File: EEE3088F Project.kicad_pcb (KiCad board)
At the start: 2 copper layers, 58 parts, among them J1 Conn_02x16_Odd_Even, J2 Battery IN JST, M1Control1 DRV8837, M2Control1 DRV8837, M3Control1 DRV8837, M4Control1 DRV8837, Q2 AO3400A, U1 TP4056, U2 TPS62163DSG, U3 MT3608, U5 TPS62162DSG, U6 CH224K

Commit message: changed inductors
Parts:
- removed L3: 2.2uH, Inductor_SMD:L_Taiyo-Yuden_MD-3030
- added L4: 3.3uH, Custom Footprints:IND-SMD_L4.0-W4.0_FNR40XXS, F.Cu at (156.6, 91.3)
- added OverCurrentFlag2TP1: TestPoint, TestPoint:TestPoint_Pad_2.0x2.0mm, F.Cu at (155.8, 77.1)
- added OvercurrentFlag1TP1: TestPoint, TestPoint:TestPoint_Pad_2.0x2.0mm, F.Cu at (155.8, 81.1)
- added TP1: 5V_test, TestPoint:TestPoint_Pad_2.0x2.0mm, F.Cu at (159.8, 77.1)
- added TP2: USBC9V_test, TestPoint:TestPoint_Pad_2.0x2.0mm, F.Cu at (159.8, 81.1)
- added TP3: below_10k_test, TestPoint:TestPoint_Pad_2.0x2.0mm, F.Cu at (163.9, 77.1)
- added TP4: 5V_out_test, TestPoint:TestPoint_Pad_2.0x2.0mm, F.Cu at (163.9, 81.1)
- added TP5: 3V3_out_test, TestPoint:TestPoint_Pad_2.0x2.0mm, F.Cu at (167.9, 77.1)
- added UnusedPinTP1: TestPoint, TestPoint:TestPoint_Pad_2.0x2.0mm, F.Cu at (167.9, 81.1)
- L1: value 2.2uH -> 10uH; footprint Inductor_SMD:L_Taiyo-Yuden_MD-3030 -> Custom Footprints:IND-SMD_L7.8-W7.0-A
- L2: value 2.2uH -> 3.3uH; footprint Inductor_SMD:L_Taiyo-Yuden_MD-3030 -> Custom Footprints:IND-SMD_L4.0-W4.0_FNR40XXS
- moved L1 67.1 mm to (164.3, 87.5)
- moved L2 64.4 mm to (156.6, 85.9)
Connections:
- net /5V_out renamed /5V Regulated
- C11 pad 2: Net-(JP2-B) -> /3V3 Regulated
- C15 pad 1: /3V3_out -> /3V3 Regulated
- C2 pad 1: VBatt -> VCharge
- C3 pad 1: VBUS -> 9V USB-C
- C6 pad 2: Net-(JP2-B) -> /3V3 Regulated
- C7 pad 2: Net-(JP2-B) -> /3V3 Regulated
- C9 pad 2: Net-(JP2-B) -> /3V3 Regulated
- CurrentSensor1 pad 2: VBatt -> /RSense-
- J1 pad 12: unconnected-(J1-Pin_12-Pad12) -> /USART2_TX
- J1 pad 15: unconnected-(J1-Pin_15-Pad15) -> Net-(J1-Pin_15)
- J1 pad 18: /3V3_out -> /3V3 Regulated
- J1 pad 22: unconnected-(J1-Pin_22-Pad22) -> 9V USB-C
- J1 pad 23: unconnected-(J1-Pin_23-Pad23) -> GND
- J1 pad 9: unconnected-(J1-Pin_9-Pad9) -> /USART2_RX
- J2 pad 2: Net-(J2-Pin_2) -> /RSense+
- L1 pad 1: Net-(U2-SW) -> VBatt
- L1 pad 2: Net-(D2-A) -> Net-(D1-A)
- L2 pad 2: /3V3_out -> /3V3 Regulated
- M1Control1 pad 8: Net-(JP2-B) -> /3V3 Regulated
- M2Control1 pad 8: Net-(JP2-B) -> /3V3 Regulated
- M3Control1 pad 8: Net-(JP2-B) -> /3V3 Regulated
- M4Control1 pad 8: Net-(JP2-B) -> /3V3 Regulated
- R6 pad 1: VBUS -> 9V USB-C
- R7 pad 2: /3V3_out -> /3V3 Regulated
- RSense1 pad 1: VBatt -> /RSense-
- RSenseTP-1 pad 1: VBatt -> /RSense-
- SWPwr1 pad 1: /RSense+ -> VBatt
- SWPwr1 pad 2: Net-(J2-Pin_2) -> /RSense-
- SWPwr1 pad 3: Net-(SWPwr1-C) -> VCharge
- U1 pad 5: VBatt -> VCharge
- U2 pad 2: VBUS -> 9V USB-C
- U2 pad 3: VBUS -> 9V USB-C
- U5 pad 6: /3V3_out -> /3V3 Regulated

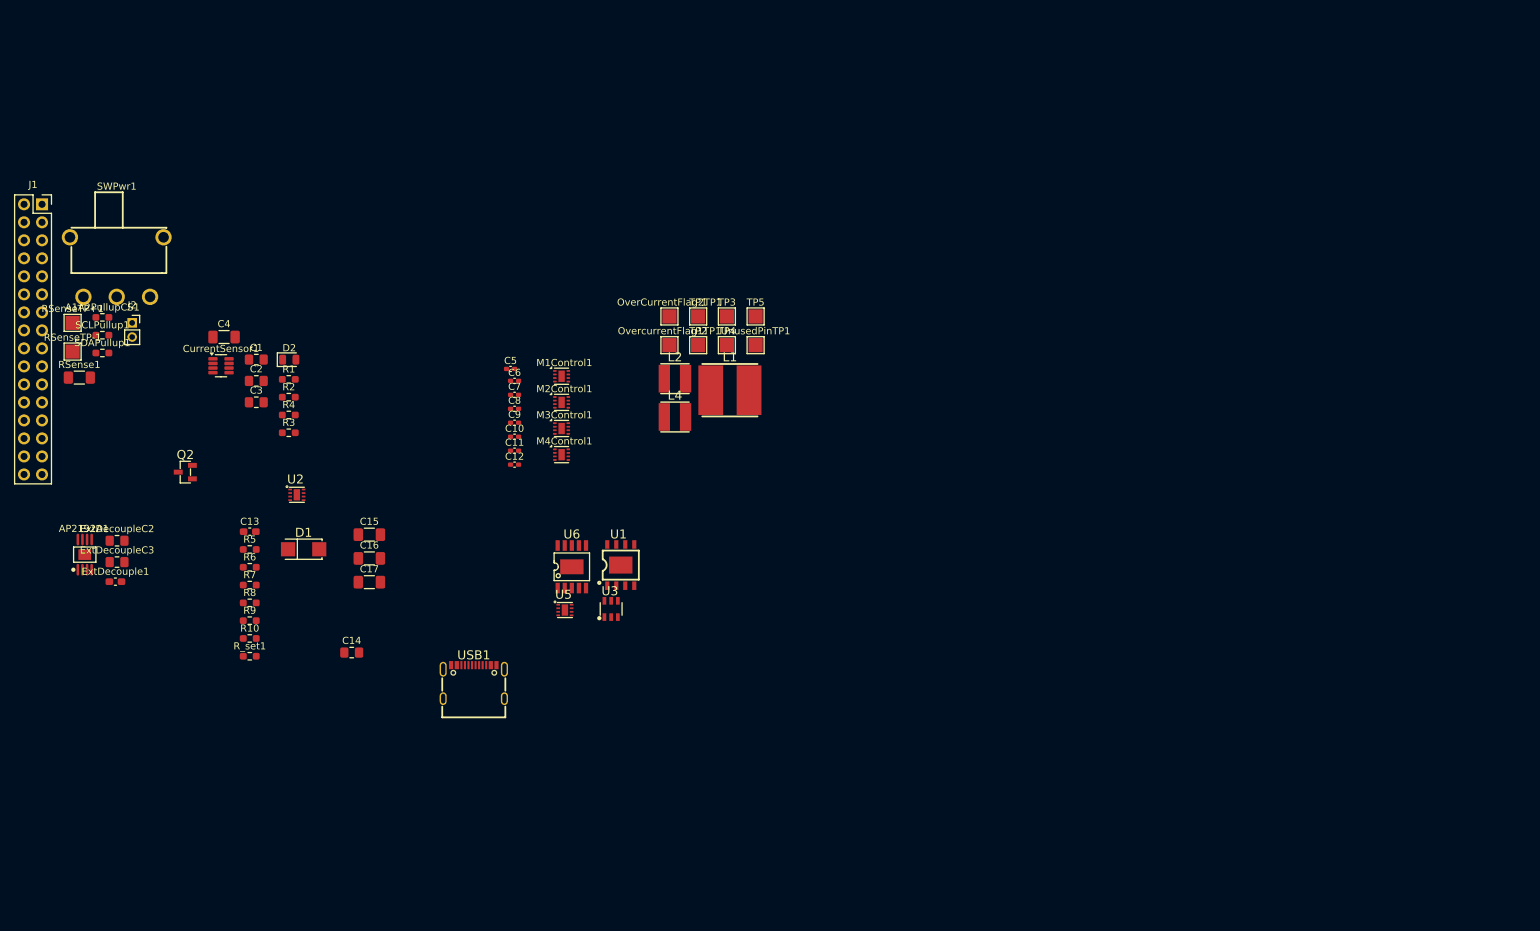
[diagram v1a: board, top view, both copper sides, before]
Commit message: Routed Thomas half of PCB traces. Minor labelling modifications in schematic.
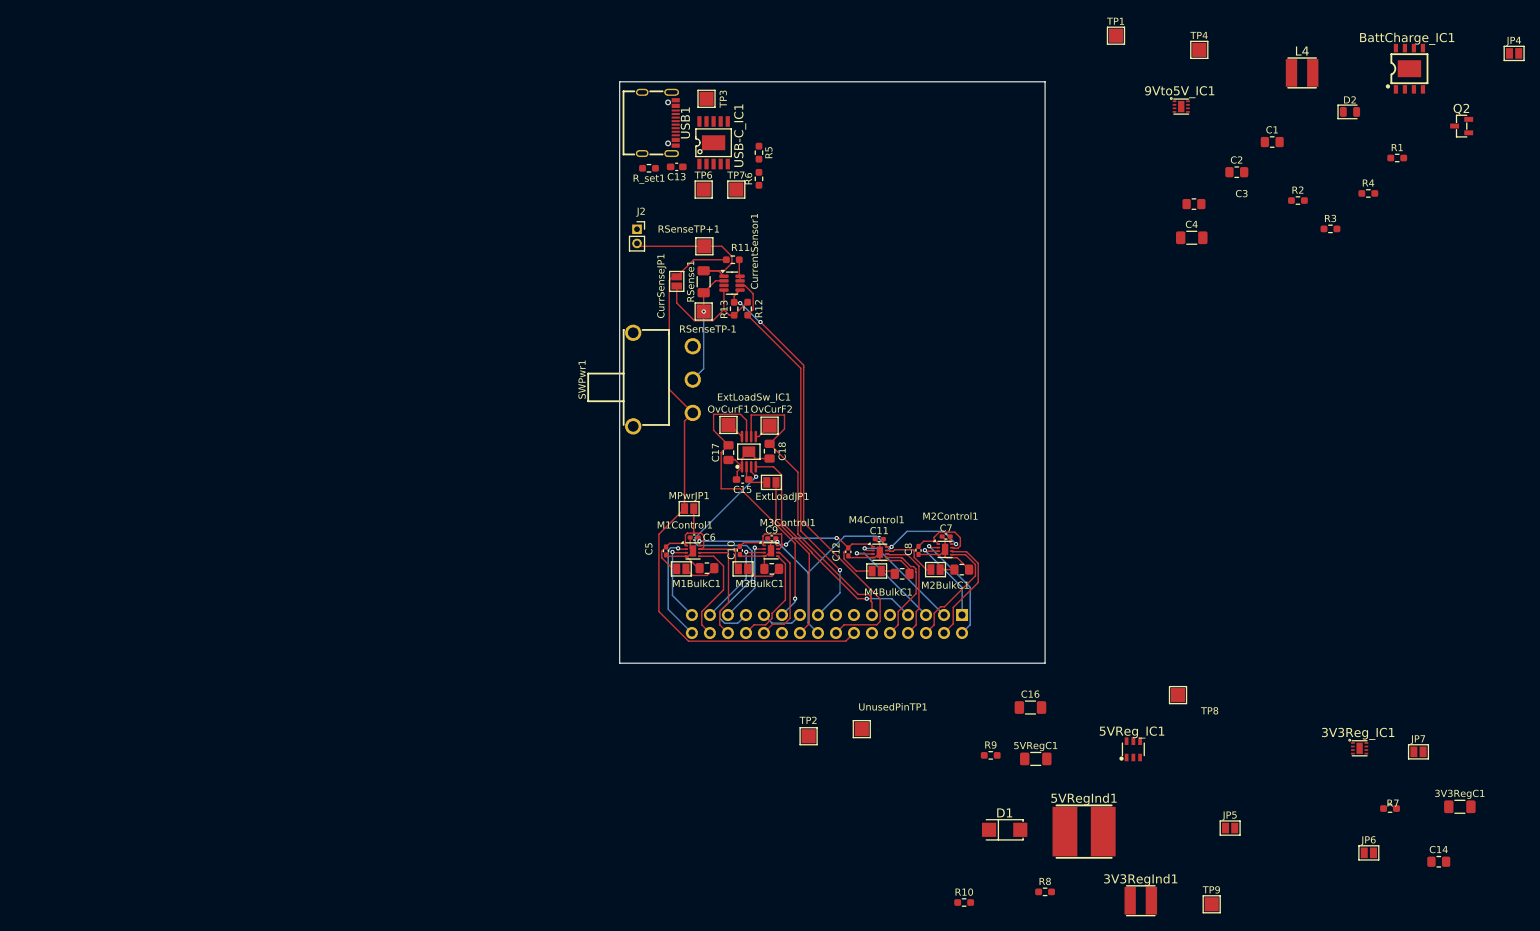
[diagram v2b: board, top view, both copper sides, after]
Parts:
- removed TP5: 3V3_out_test, TestPoint:TestPoint_Pad_2.0x2.0mm
- added CurrSenseJP1: CurrentSenseJP, Jumper:SolderJumper-2_P1.3mm_Open_Pad1.0x1.5mm, F.Cu at (156.8, 72.2)
- added ExtLoadJP1: ExtLoadJP, Jumper:SolderJumper-2_P1.3mm_Open_Pad1.0x1.5mm, F.Cu at (170.2, 100.5)
- added JP10: BCM2_JP, Jumper:SolderJumper-2_P1.3mm_Open_Pad1.0x1.5mm, F.Cu at (193.3, 112.8)
- added JP11: BCM1_JP, Jumper:SolderJumper-2_P1.3mm_Open_Pad1.0x1.5mm, F.Cu at (157.4, 112.7)
- added JP4: ChargeJP, Jumper:SolderJumper-2_P1.3mm_Open_Pad1.0x1.5mm, F.Cu at (274.9, 40.0)
- added JP5: 5VRegInJP, Jumper:SolderJumper-2_P1.3mm_Open_Pad1.0x1.5mm, F.Cu at (234.8, 149.2)
- added JP6: 3V3RegInJP, Jumper:SolderJumper-2_P1.3mm_Open_Pad1.0x1.5mm, F.Cu at (254.4, 152.8)
- added JP7: 3V3RegOutJP, Jumper:SolderJumper-2_P1.3mm_Open_Pad1.0x1.5mm, F.Cu at (261.4, 138.5)
- added JP8: BCM4_JP, Jumper:SolderJumper-2_P1.3mm_Open_Pad1.0x1.5mm, F.Cu at (185.0, 113.0)
- added M1BulkC1: 10uF, Capacitor_SMD:C_0805_2012Metric_Pad1.18x1.45mm_HandSolder, F.Cu at (161.1, 112.6)
- added M2BulkC1: 10uF, Capacitor_SMD:C_0805_2012Metric_Pad1.18x1.45mm_HandSolder, F.Cu at (197.0, 112.8)
- added M3BC1: BCM3_JP, Jumper:SolderJumper-2_P1.3mm_Open_Pad1.0x1.5mm, F.Cu at (166.2, 112.7)
- added M3BulkC1: 10uF, Capacitor_SMD:C_0805_2012Metric_Pad1.18x1.45mm_HandSolder, F.Cu at (170.2, 112.7)
- added M4BulkC1: 10uF, Capacitor_SMD:C_0805_2012Metric_Pad1.18x1.45mm_HandSolder, F.Cu at (188.6, 113.4)
- added MPwrJP1: MotorPWRJP, Jumper:SolderJumper-2_P1.3mm_Open_Pad1.0x1.5mm, F.Cu at (158.6, 104.2)
- added TP6: DP_TP, TestPoint:TestPoint_Pad_2.0x2.0mm, F.Cu at (160.6, 59.2)
- added TP7: DM_TP, TestPoint:TestPoint_Pad_2.0x2.0mm, F.Cu at (165.2, 59.2)
- added TP8: 5VRegDiv_TP2, TestPoint:TestPoint_Pad_2.0x2.0mm, F.Cu at (227.5, 130.5)
- added TP9: 5VRegDiv_TP1, TestPoint:TestPoint_Pad_2.0x2.0mm, F.Cu at (232.2, 160.0)
- J1: moved to B.Cu
- TP1: value 5V_test -> 5V_TP
- TP2: value USBC9V_test -> USBC9V_TP
- TP3: value below_10k_test -> below_10k_TP
- moved Q2 186.5 mm to (267.5, 50.2)
- moved R7 163.9 mm to (257.4, 146.5)
- moved R1 159.4 mm to (258.4, 54.8)
- moved 3V3RegC1 158.5 mm to (267.2, 146.2)
- moved C14 156.1 mm to (264.3, 154.0)
- moved R4 155.4 mm to (254.3, 59.8)
- moved D2 153.6 mm to (251.8, 48.2)
- moved R3 149.7 mm to (249.0, 64.8)
- moved C1 146.5 mm to (240.8, 52.5)
- moved R2 145.0 mm to (244.4, 60.8)
- moved J1 142.1 mm to (197.0, 119.2), turned to 90 degrees
- moved C2 141.4 mm to (235.8, 56.8)
- moved C4 137.2 mm to (229.4, 66.0)
- moved 9Vto5V_IC1 136.2 mm to (227.9, 47.5)
- moved C3 135.2 mm to (229.8, 61.2)
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- renumbered C15 to 3V3RegC1, L2 to 3V3RegInd1, U5 to 3V3Reg_IC1, C17 to 5VRegC1, L1 to 5VRegInd1, U3 to 5VReg_IC1, U2 to 9Vto5V_IC1, U1 to BattCharge_IC1, ExtDecouple1 to C15, ExtDecoupleC2 to C17, ExtDecoupleC3 to C18, AP2192A1 to ExtLoadSw_IC1, OvercurrentFlag1TP1 to OvCurF1, OverCurrentFlag2TP1 to OvCurF2, A1A2PullupCS1 to R11, SDAPullup1 to R12, SCLPullup1 to R13, U6 to USB-C_IC1
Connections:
- 3V3RegC1 pad 1: /3V3 Regulated -> Net-(3V3Reg_IC1-VOS)
- 3V3RegInd1 pad 2: /3V3 Regulated -> Net-(3V3Reg_IC1-VOS)
- 3V3Reg_IC1 pad 2: /5V Regulated -> Net-(3V3Reg_IC1-EN)
- 3V3Reg_IC1 pad 3: /5V Regulated -> Net-(3V3Reg_IC1-EN)
- 3V3Reg_IC1 pad 6: /3V3 Regulated -> Net-(3V3Reg_IC1-VOS)
- 5VRegInd1 pad 1: VBatt -> Net-(5VReg_IC1-EN)
- 5VReg_IC1 pad 4: VBatt -> Net-(5VReg_IC1-EN)
- 5VReg_IC1 pad 5: VBatt -> Net-(5VReg_IC1-EN)
- 9Vto5V_IC1 pad 2: 9V USB-C -> Net-(9Vto5V_IC1-EN)
- 9Vto5V_IC1 pad 3: 9V USB-C -> Net-(9Vto5V_IC1-EN)
- C10 pad 1: Net-(JP2-B) -> Net-(JP10-A)
- C12 pad 1: Net-(JP2-B) -> Net-(JP10-A)
- C14 pad 1: /5V Regulated -> Net-(3V3Reg_IC1-EN)
- C16 pad 1: VBatt -> Net-(5VReg_IC1-EN)
- C3 pad 1: 9V USB-C -> Net-(9Vto5V_IC1-EN)
- C5 pad 1: Net-(JP2-B) -> Net-(JP10-A)
- C8 pad 1: Net-(JP2-B) -> Net-(JP10-A)
- J1 pad 1: /MOTOR2_B_OUT -> /MOTOR2_B_OUT 
- J1 pad 19: unconnected-(J1-Pin_19-Pad19) -> GND
- J1 pad 6: /MOTOR2_CTRL2  -> /MOTOR2_CTRL2
- J1 pad 8: /MOTOR4_CTRL1  -> /MOTOR4_CTRL1
- M1Control1 pad 1: Net-(JP2-B) -> Net-(JP10-A)
- M1Control1 pad 7: VBatt -> Net-(JP10-A)
- M2Control1 pad 1: Net-(JP2-B) -> Net-(JP10-A)
- M2Control1 pad 7: VBatt -> Net-(JP10-A)
- M3Control1 pad 1: Net-(JP2-B) -> Net-(JP10-A)
- M3Control1 pad 7: VBatt -> Net-(JP10-A)
- M4Control1 pad 1: Net-(JP2-B) -> Net-(JP10-A)
- M4Control1 pad 3: /MOTOR4_B_OUT  -> /MOTOR4_B_OUT
- M4Control1 pad 7: VBatt -> Net-(JP10-A)
- R7 pad 2: /3V3 Regulated -> Net-(3V3Reg_IC1-VOS)
- USB-C_IC1 pad 4: unconnected-(U6-DP-Pad4) -> Net-(USB-C_IC1-DP)
- USB-C_IC1 pad 5: unconnected-(U6-DM-Pad5) -> Net-(USB-C_IC1-DM)
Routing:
- net VBatt: track 0.00 -> 89.0 mm
- net Net-(JP10-A): track 0.00 -> 77.0 mm, vias 0 -> 2
- net /12C1_SCL: track 0.00 -> 63.3 mm, vias 0 -> 2
- net /3V3 Regulated: track 0.00 -> 60.6 mm, vias 0 -> 4
- net GND: track 0.00 -> 58.5 mm
- net /12C1_SDA: track 0.00 -> 54.6 mm, vias 0 -> 1
- net /EXT_LOAD2_OUT: track 0.00 -> 43.7 mm
- net /EXT_LOAD1_OUT: track 0.00 -> 43.6 mm, vias 0 -> 1
- net /CTRL_EXT_LOAD1: track 0.00 -> 38.9 mm, vias 0 -> 1
- net /CTRL_EXT_LOAD2: track 0.00 -> 34.1 mm, vias 0 -> 1
- net /5V Regulated: track 0.00 -> 23.7 mm
- net /RSense+: track 0.00 -> 22.7 mm
- net Net-(CurrSenseJP1-A): track 0.00 -> 17.9 mm
- net /MOTOR2_CTRL2: track 0.00 -> 16.7 mm
- net /MOTOR2_A_OUT: track 0.00 -> 16.5 mm, vias 0 -> 1
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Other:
- board outline added: 60 x 82 mm

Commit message: finished routing
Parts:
- moved C14 104.5 mm to (178.0, 95.1), turned to -90 degrees
- moved 3V3RegPinJP 98.8 mm to (179.5, 88.3), turned to 90 degrees
- moved ChargeJP 96.6 mm to (179.3, 54.0)
- moved 5VRegInJP 94.9 mm to (176.3, 74.5), turned to 180 degrees
- moved 3V3RegC1 90.4 mm to (194.2, 93.0), turned to -90 degrees
- moved R7 88.2 mm to (185.5, 95.3), turned to -90 degrees
- moved 5VRegDiv_TP1 85.4 mm to (200.5, 80.8)
- moved USBC9V_TP 85.1 mm to (173.2, 51.2)
- moved 3V3Reg_IC1 83.0 mm to (181.9, 95.3)
- moved R1 82.3 mm to (176.9, 66.5)
- moved BattCharge_IC1 79.2 mm to (184.0, 64.0), turned to 90 degrees
- moved CHRG_LED 76.8 mm to (176.5, 63.5), turned to 90 degrees
- moved 5VRegInd1 76.6 mm to (197.5, 75.0)
- moved 3V3RegInd1 76.0 mm to (189.2, 91.0)
- moved AO3400A 75.4 mm to (193.5, 64.5), turned to -90 degrees
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- renumbered JP7 to 3V3RegOutJP, JP6 to 3V3RegPinJP, TP4 to 5VOutTest_TP, TP9 to 5VRegDiv_TP1, TP8 to 5VRegDiv_TP2, JP5 to 5VRegInJP, TP1 to 5V_TP, Q2 to AO3400A, D2 to CHRG_LED, JP4 to ChargeJP, TP7 to DM_TP, TP6 to DP_TP, D1 to D_S, USB-C_IC1 to USB-C_IC, USB1 to USB-TYPEC-16PIN, TP2 to USBC9V_TP, TP3 to below_10k_TP
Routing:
- net GND: track 58.5 -> 226.3 mm, vias 0 -> 10
- net 9V USB-C: track 0.00 -> 133.9 mm, vias 0 -> 1
- net /FAST_CHRG_CNTRL: track 0.00 -> 130.3 mm, vias 0 -> 1
- net Net-(9Vto5V_IC1-VOS): track 0.00 -> 68.4 mm, vias 0 -> 2
- net /5V Regulated: track 23.7 -> 91.7 mm, vias 0 -> 4
- net VCharge: track 0.00 -> 67.3 mm, vias 0 -> 4
- net /3V3 Regulated: track 60.6 -> 122.5 mm, vias 4 -> 7
- net Net-(5VReg_IC1-SW): track 0.00 -> 43.2 mm, vias 0 -> 2
- net Net-(5VReg_IC1-FB): track 0.00 -> 40.0 mm
- net Net-(3V3Reg_IC1-VOS): track 0.00 -> 35.7 mm
- net Net-(J1-Pin_15): track 0.00 -> 32.0 mm, vias 0 -> 2
- net Net-(USB-C_IC1-VBUS): track 0.00 -> 28.3 mm
- net /VBUS_USBC: track 0.00 -> 22.9 mm
- net Net-(5VReg_IC1-EN): track 0.00 -> 20.3 mm
- net VBatt: track 89.0 -> 109.1 mm, vias 0 -> 4
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
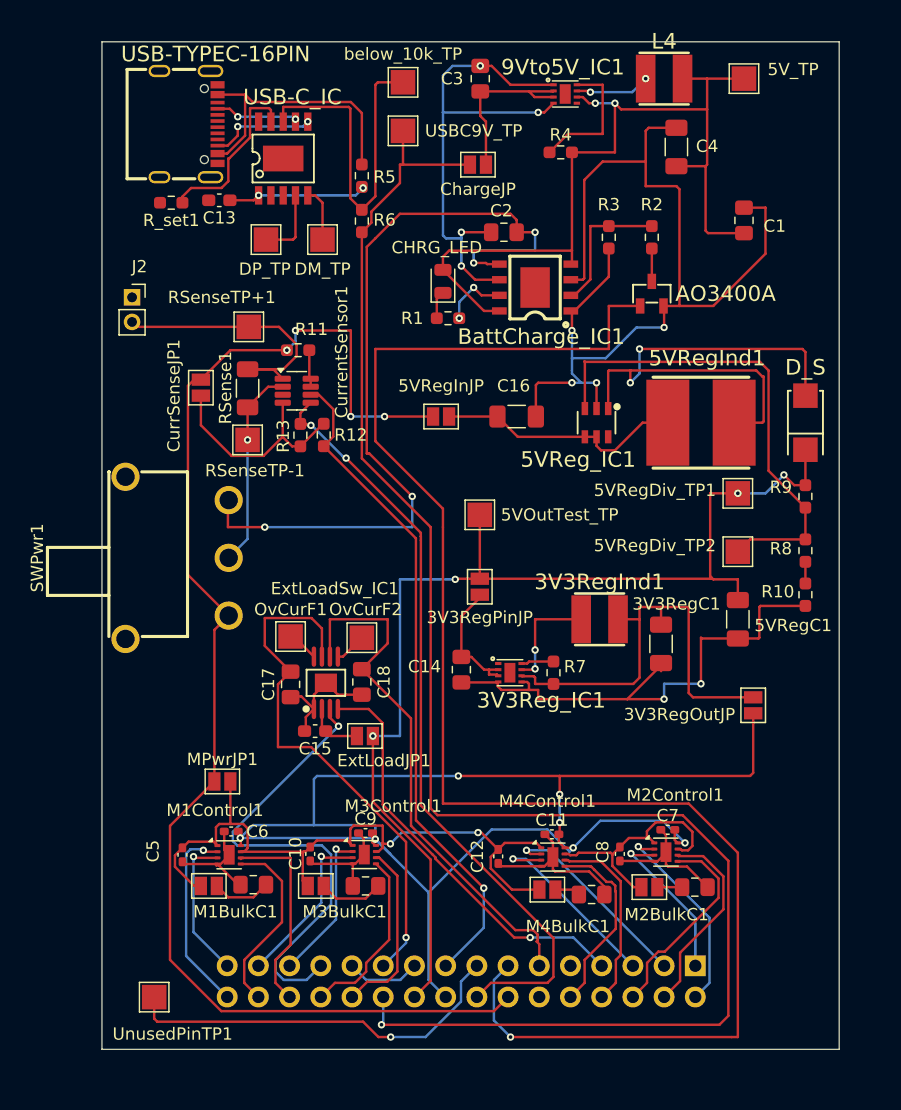
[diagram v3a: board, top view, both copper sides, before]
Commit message: added and fixed traces and trace widths. Fixed design rule check errors
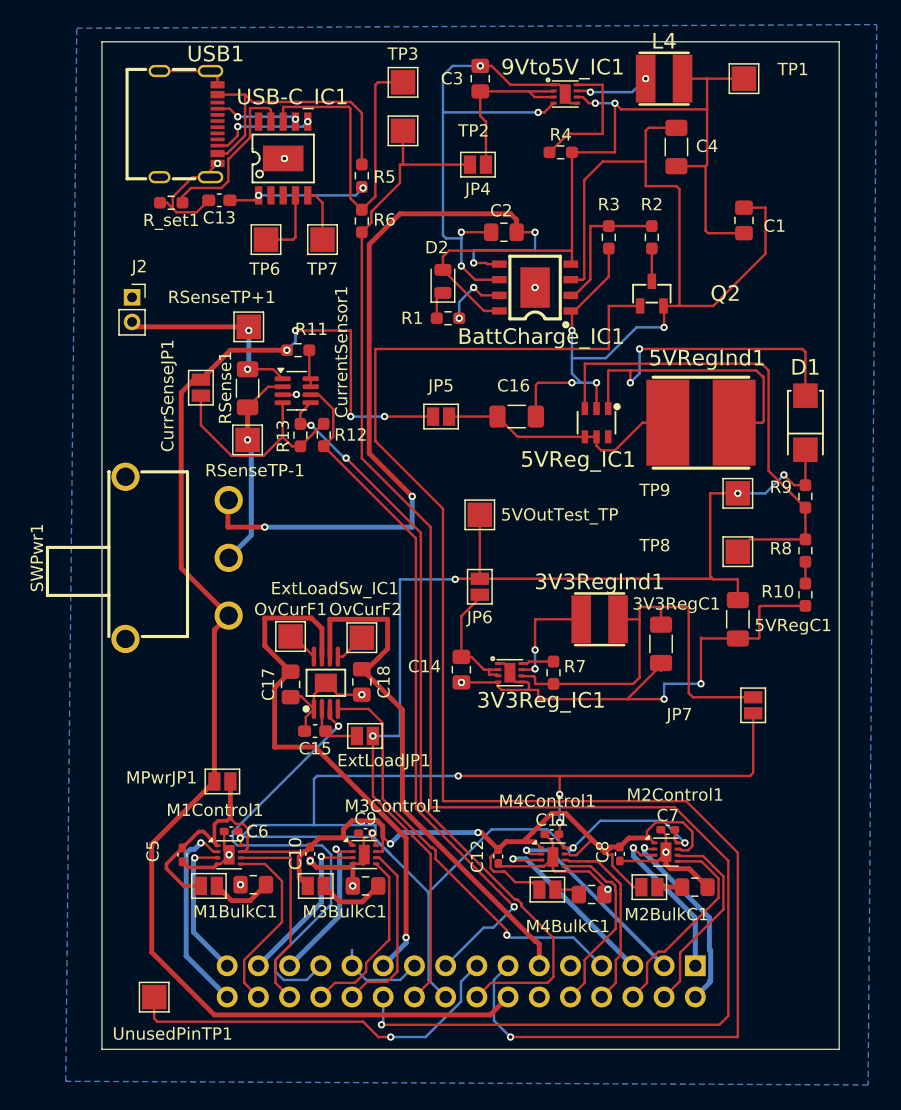
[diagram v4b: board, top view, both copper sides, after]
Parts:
- renumbered M3BC1 to BCM3_JP1, D_S to D1, CHRG_LED to D2, ChargeJP to JP4, 5VRegInJP to JP5, 3V3RegPinJP to JP6, 3V3RegOutJP to JP7, AO3400A to Q2, 5V_TP to TP1, USBC9V_TP to TP2, below_10k_TP to TP3, DP_TP to TP6, DM_TP to TP7, 5VRegDiv_TP2 to TP8, 5VRegDiv_TP1 to TP9, USB-C_IC to USB-C_IC1, USB-TYPEC-16PIN to USB1
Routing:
- net GND: track 226.3 -> 251.2 mm, vias 10 -> 22
- net Net-(BCM3_JP1-A): track 77.0 -> 89.3 mm
- net /RSense+: track 22.7 -> 16.3 mm, vias 0 -> 2
- net /12C1_SDA: track 54.6 -> 57.1 mm
- net VBatt: track 109.1 -> 111.6 mm
- net /MOTOR2_A_OUT: track 16.5 -> 15.8 mm
- net /EXT_LOAD2_OUT: track 43.7 -> 43.1 mm
- net /EXT_LOAD1_OUT: track 43.6 -> 44.1 mm
- net Net-(J1-Pin_15): vias 2 -> 1
- added copper zone on B.Cu, net GND
